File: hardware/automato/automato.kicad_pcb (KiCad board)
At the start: 2 copper layers, 100 x 55.5 mm, 25 parts, among them J2 Motor_L, J3 Motor_3, J5 Servo 1, J6 i2c, U1 ESP32-C6-DEVKITC-1-N8, U2 DRV8411APWPR, U3 AP63357DV-7

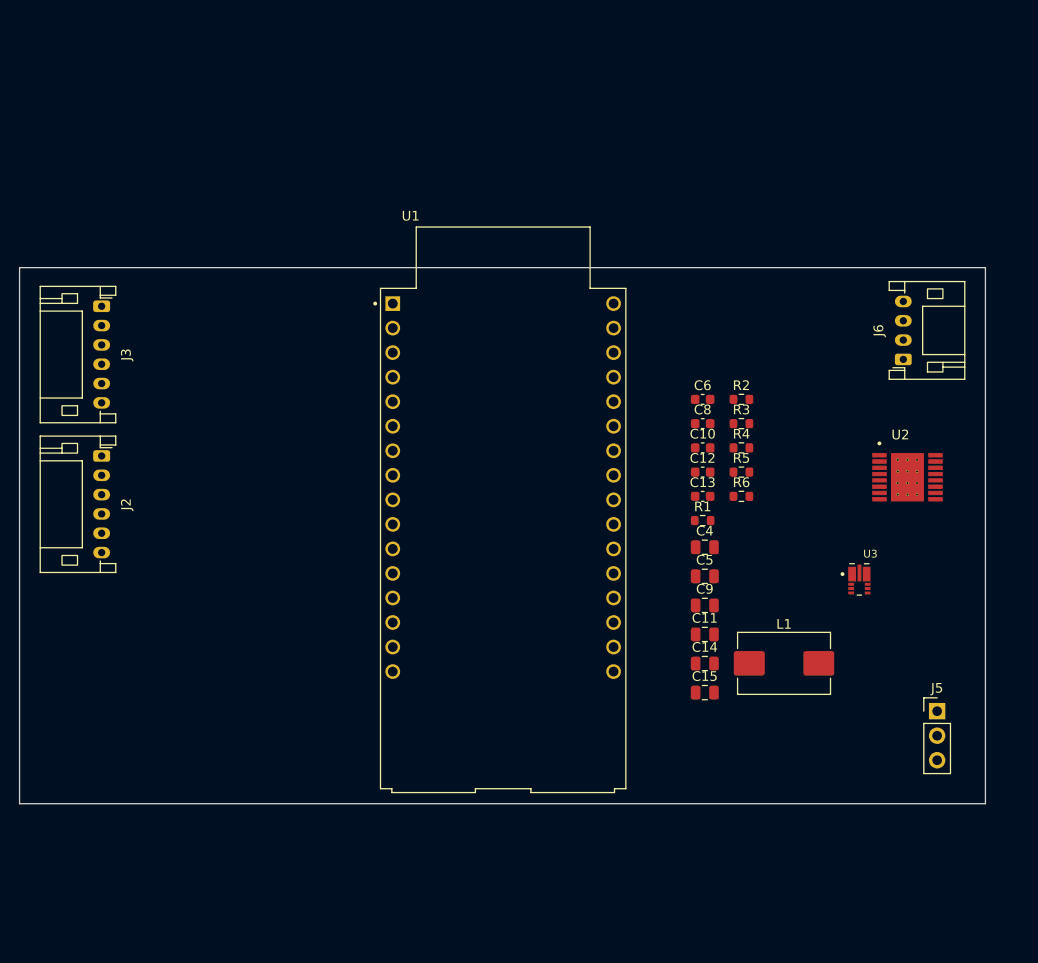
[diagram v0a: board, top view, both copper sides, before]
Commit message: added relays and mosfets
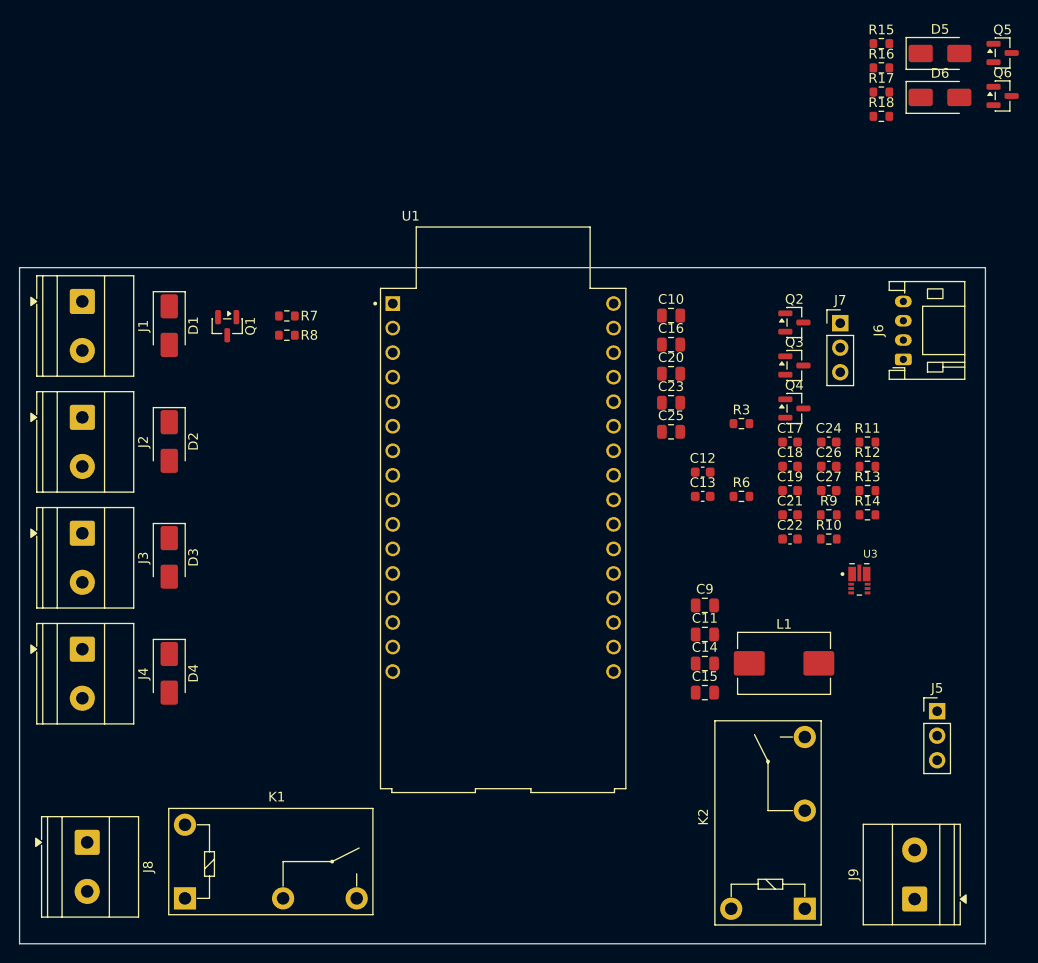
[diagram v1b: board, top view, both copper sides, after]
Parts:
- removed C4, C5: 22uF, Capacitor_SMD:C_0805_2012Metric
- removed C6, C8: 0.1uf, Capacitor_SMD:C_0603_1608Metric
- removed R1, R2: 100k, Resistor_SMD:R_0603_1608Metric
- removed R4, R5: 5.1k, Resistor_SMD:R_0603_1608Metric
- removed U2: DRV8411APWPR, Kjelland:IC_DRV8411APWPR
- added C16: 22uF, Capacitor_SMD:C_0805_2012Metric, F.Cu at (167.9, 102.5)
- added C17: 0.1uF, Capacitor_SMD:C_0603_1608Metric, F.Cu at (180.3, 112.6)
- added C18: 0.1uF, Capacitor_SMD:C_0603_1608Metric, F.Cu at (180.3, 115.1)
- added C19: 0.1uF, Capacitor_SMD:C_0603_1608Metric, F.Cu at (180.3, 117.6)
- added C20: 22uF, Capacitor_SMD:C_0805_2012Metric, F.Cu at (167.9, 105.5)
- added C21: 0.1uF, Capacitor_SMD:C_0603_1608Metric, F.Cu at (180.3, 120.1)
- added C22: 0.1uF, Capacitor_SMD:C_0603_1608Metric, F.Cu at (180.3, 122.6)
- added C23: 22uF, Capacitor_SMD:C_0805_2012Metric, F.Cu at (167.9, 108.5)
- added C24: 0.1uF, Capacitor_SMD:C_0603_1608Metric, F.Cu at (184.3, 112.6)
- added C25: 22uF, Capacitor_SMD:C_0805_2012Metric, F.Cu at (167.9, 111.5)
- added C26: 0.1uF, Capacitor_SMD:C_0603_1608Metric, F.Cu at (184.3, 115.1)
- added C27: 0.1uF, Capacitor_SMD:C_0603_1608Metric, F.Cu at (184.3, 117.6)
- added D1: SS34, Diode_SMD:D_SMA, F.Cu at (116.0, 100.5)
- added D2: SS34, Diode_SMD:D_SMA, F.Cu at (116.0, 112.5)
- added D3: SS34, Diode_SMD:D_SMA, F.Cu at (116.0, 124.5)
- added D4: SS34, Diode_SMD:D_SMA, F.Cu at (116.0, 136.5)
- added D5: SS34, Diode_SMD:D_SMA, F.Cu at (195.8, 72.3)
- added D6: SS34, Diode_SMD:D_SMA, F.Cu at (195.8, 76.9)
- added J1: Motor1, TerminalBlock_Phoenix:TerminalBlock_Phoenix_MKDS-1,5-2-5.08_1x02_P5.08mm_Horizontal, F.Cu at (107.0, 98.0)
- added J4: Motor3, TerminalBlock_Phoenix:TerminalBlock_Phoenix_MKDS-1,5-2-5.08_1x02_P5.08mm_Horizontal, F.Cu at (107.0, 134.0)
- added J7: Servo 2, Connector_PinHeader_2.54mm:PinHeader_1x03_P2.54mm_Vertical, F.Cu at (185.5, 100.2)
- added J8: Relay 1, TerminalBlock_Phoenix:TerminalBlock_Phoenix_MKDS-1,5-2-5.08_1x02_P5.08mm_Horizontal, F.Cu at (107.5, 154.0)
- added J9: Relay 2, TerminalBlock_Phoenix:TerminalBlock_Phoenix_MKDS-1,5-2-5.08_1x02_P5.08mm_Horizontal, F.Cu at (193.2, 159.9)
- added K1: G5Q-1A, Relay_THT:Relay_SPST_Omron-G5Q-1A, F.Cu at (117.6, 159.8)
- added K2: G5Q-1A, Relay_THT:Relay_SPST_Omron-G5Q-1A, F.Cu at (181.8, 160.9)
- added Q1: AO3400A, Package_TO_SOT_SMD:SOT-23, F.Cu at (122.0, 100.6)
- added Q2: AO3400A, Package_TO_SOT_SMD:SOT-23, F.Cu at (180.7, 100.2)
- added Q3: AO3400A, Package_TO_SOT_SMD:SOT-23, F.Cu at (180.7, 104.6)
- added Q4: AO3400A, Package_TO_SOT_SMD:SOT-23, F.Cu at (180.7, 109.1)
- added Q5: AO3400A, Package_TO_SOT_SMD:SOT-23, F.Cu at (202.3, 72.3)
- added Q6: AO3400A, Package_TO_SOT_SMD:SOT-23, F.Cu at (202.3, 76.7)
- added R10: 10k, Resistor_SMD:R_0603_1608Metric, F.Cu at (184.3, 122.6)
- added R11: 120R, Resistor_SMD:R_0603_1608Metric, F.Cu at (188.3, 112.6)
- added R12: 10k, Resistor_SMD:R_0603_1608Metric, F.Cu at (188.3, 115.1)
- added R13: 120R, Resistor_SMD:R_0603_1608Metric, F.Cu at (188.3, 117.6)
- added R14: 10k, Resistor_SMD:R_0603_1608Metric, F.Cu at (188.3, 120.1)
- added R15: 120R, Resistor_SMD:R_0603_1608Metric, F.Cu at (189.7, 71.3)
- added R16: 10k, Resistor_SMD:R_0603_1608Metric, F.Cu at (189.7, 73.8)
- added R17: 120R, Resistor_SMD:R_0603_1608Metric, F.Cu at (189.7, 76.3)
- added R18: 10k, Resistor_SMD:R_0603_1608Metric, F.Cu at (189.7, 78.8)
- added R7: 120R, Resistor_SMD:R_0603_1608Metric, F.Cu at (128.2, 99.5)
- added R8: 10k, Resistor_SMD:R_0603_1608Metric, F.Cu at (128.2, 101.5)
- added R9: 120R, Resistor_SMD:R_0603_1608Metric, F.Cu at (184.3, 120.1)
- C10: value 0.1uf -> 22uF; footprint Capacitor_SMD:C_0603_1608Metric -> Capacitor_SMD:C_0805_2012Metric
- J2: value Motor_L -> Motor2; footprint Connector_JST:JST_PH_S6B-PH-K_1x06_P2.00mm_Horizontal -> TerminalBlock_Phoenix:TerminalBlock_Phoenix_MKDS-1,5-2-5.08_1x02_P5.08mm_Horizontal
- J3: value Motor_3 -> Motor4; footprint Connector_JST:JST_PH_S6B-PH-K_1x06_P2.00mm_Horizontal -> TerminalBlock_Phoenix:TerminalBlock_Phoenix_MKDS-1,5-2-5.08_1x02_P5.08mm_Horizontal
- moved J3 23.6 mm to (107.0, 122.0)
- moved C10 14.1 mm to (167.9, 99.5)
- moved J2 4.47 mm to (107.0, 110.0)
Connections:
- C10 pad 1: /MOTOR_L_A -> +5V
- C11 pad 1: +9V -> +12V
- J2 pad 1: /MOTOR_L_OUT+ -> +12V
- J2 pad 2: /MOTOR_L_OUT- -> Net-(D2-A)
- J3 pad 1: /MOTOR_3_OUT+ -> +12V
- J3 pad 2: /MOTOR_3_OUT- -> Net-(D3-A)
- J5 pad 1: /SERVO_1 -> SERVO_1
- U1 pad J1_12: /ENC_LB -> unconnected-(U1-GPIO14-PadJ1_12)
- U1 pad J1_3: /SERVO_1 -> SERVO_2
- U1 pad J1_4: unconnected-(U1-GPIO3-PadJ1_4) -> MOTOR_1
- U1 pad J1_5: unconnected-(U1-GPIO4-PadJ1_5) -> MOTOR_2
- U1 pad J1_6: unconnected-(U1-GPIO5-PadJ1_6) -> MOTOR_3
- U1 pad J1_7: /MOTOR_L_A -> MOTOR_4
- U1 pad J1_8: /MOTOR_3_A -> SERVO_1
- U1 pad J1_9: /ENC_LA -> unconnected-(U1-GPIO8-PadJ1_9)
- U1 pad J3_4: /ENC_3A -> unconnected-(U1-GPIO23-PadJ3_4)
- U1 pad J3_5: /ENC_3B -> unconnected-(U1-GPIO22-PadJ3_5)
- U1 pad J3_6: /MOTOR_3_IN2 -> unconnected-(U1-GPIO21-PadJ3_6)
- U1 pad J3_7: /MOTOR_3_IN1 -> unconnected-(U1-GPIO20-PadJ3_7)
- U1 pad J3_8: /MOTOR_L_IN2 -> unconnected-(U1-GPIO19-PadJ3_8)
- U1 pad J3_9: /MOTOR_L_IN1 -> unconnected-(U1-GPIO18-PadJ3_9)
- U3 pad 1: +9V -> +12V
- U3 pad 2: +9V -> +12V
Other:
- board size 100 x 55.5 mm -> 100 x 70 mm

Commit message: started layout
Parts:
- added C28: 22uF, Capacitor_SMD:C_0805_2012Metric, F.Cu at (236.5, 66.0)
- added C29: 22uF, Capacitor_SMD:C_0805_2012Metric, F.Cu at (236.5, 71.0)
- added FID1: Fiducial, Fiducial:Fiducial_1.5mm_Mask3mm, F.Cu at (233.5, 47.0)
- added FID2: Fiducial, Fiducial:Fiducial_1.5mm_Mask3mm, F.Cu at (161.0, 45.5)
- added FID3: Fiducial, Fiducial:Fiducial_1.5mm_Mask3mm, F.Cu at (242.5, 119.5)
- added FID4: Fiducial, Fiducial:Fiducial_1.5mm_Mask3mm, F.Cu at (182.0, 128.0)
- added H1: MountingHole, MountingHole:MountingHole_3.2mm_M3, F.Cu at (152.0, 129.0)
- added H2: MountingHole, MountingHole:MountingHole_3.2mm_M3, F.Cu at (152.0, 45.0)
- added H3: MountingHole, MountingHole:MountingHole_3.2mm_M3, F.Cu at (246.0, 45.0)
- added H4: MountingHole, MountingHole:MountingHole_3.2mm_M3, F.Cu at (246.0, 129.0)
- added J10: Servo 3, Connector_PinHeader_2.54mm:PinHeader_1x03_P2.54mm_Vertical, F.Cu at (241.9, 66.0)
- added J11: Servo 4, Connector_PinHeader_2.54mm:PinHeader_1x03_P2.54mm_Vertical, F.Cu at (241.9, 71.0)
- added J12: Barrel_Jack, Connector_BarrelJack:BarrelJack_Horizontal, F.Cu at (163.0, 120.3)
- added R19: 4.7k, Resistor_SMD:R_0603_1608Metric, F.Cu at (163.5, 108.0)
- added R20: 4.7k, Resistor_SMD:R_0603_1608Metric, F.Cu at (163.5, 105.0)
- moved J8 114.1 mm to (217.0, 122.0), turned to 0 degrees
- moved C17 109.2 mm to (97.3, 41.6)
- moved C19 109.2 mm to (97.3, 46.6)
- moved C22 109.2 mm to (97.3, 51.6)
- moved C16 109.2 mm to (85.0, 31.5)
- moved C20 109.2 mm to (85.0, 34.5)
- moved C23 109.2 mm to (85.0, 37.5)
- moved C24 109.2 mm to (101.3, 41.6)
- moved C25 109.2 mm to (85.0, 40.5)
- moved C9 98.2 mm to (236.5, 56.0), turned to -90 degrees
- moved J5 96.3 mm to (241.9, 56.0), turned to 90 degrees
- moved K1 96.3 mm to (201.8, 113.0)
- moved C10 78.6 mm to (236.5, 61.0), turned to -90 degrees
- moved D4 74.4 mm to (165.0, 80.5)
- moved J4 74.4 mm to (156.0, 78.0)
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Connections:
- net /SCL renamed SCL
- net /SDA renamed SDA
- U1 pad J1_12: unconnected-(U1-GPIO14-PadJ1_12) -> RELAY_1
- U1 pad J1_13: unconnected-(U1-GND-PadJ1_13) -> GND
- U1 pad J1_15: unconnected-(U1-GND_J1_15-PadJ1_15) -> GND
- U1 pad J1_3: SERVO_2 -> SERVO_3
- U1 pad J1_4: MOTOR_1 -> SERVO_4
- U1 pad J1_5: MOTOR_2 -> unconnected-(U1-GPIO4-PadJ1_5)
- U1 pad J1_6: MOTOR_3 -> unconnected-(U1-GPIO5-PadJ1_6)
- U1 pad J1_7: MOTOR_4 -> RELAY_1
- U1 pad J1_8: SERVO_1 -> RELAY_2
- U1 pad J3_1: unconnected-(U1-GND_J3_1-PadJ3_1) -> GND
- U1 pad J3_12: unconnected-(U1-GND_J3_12-PadJ3_12) -> GND
- U1 pad J3_15: unconnected-(U1-GND_J3_15-PadJ3_15) -> GND
- U1 pad J3_4: unconnected-(U1-GPIO23-PadJ3_4) -> SERVO_1
- U1 pad J3_5: unconnected-(U1-GPIO22-PadJ3_5) -> SERVO_2
- U1 pad J3_6: unconnected-(U1-GPIO21-PadJ3_6) -> MOTOR_1
- U1 pad J3_7: unconnected-(U1-GPIO20-PadJ3_7) -> MOTOR_2
- U1 pad J3_8: unconnected-(U1-GPIO19-PadJ3_8) -> MOTOR_3
- U1 pad J3_9: unconnected-(U1-GPIO18-PadJ3_9) -> MOTOR_4
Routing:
- net GND: track 0.00 -> 8.71 mm, vias 0 -> 2
- net Net-(U3-SW): track 0.00 -> 6.16 mm, vias 0 -> 2
- net +12V: track 0.00 -> 4.26 mm
- net Net-(U3-FB): track 0.00 -> 3.11 mm
- net Net-(U3-BST): track 0.00 -> 2.78 mm
- added copper zone on F.Cu, net +12V
- added copper zone on B.Cu, net GND
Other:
- board size 100 x 70 mm -> 100 x 90 mm

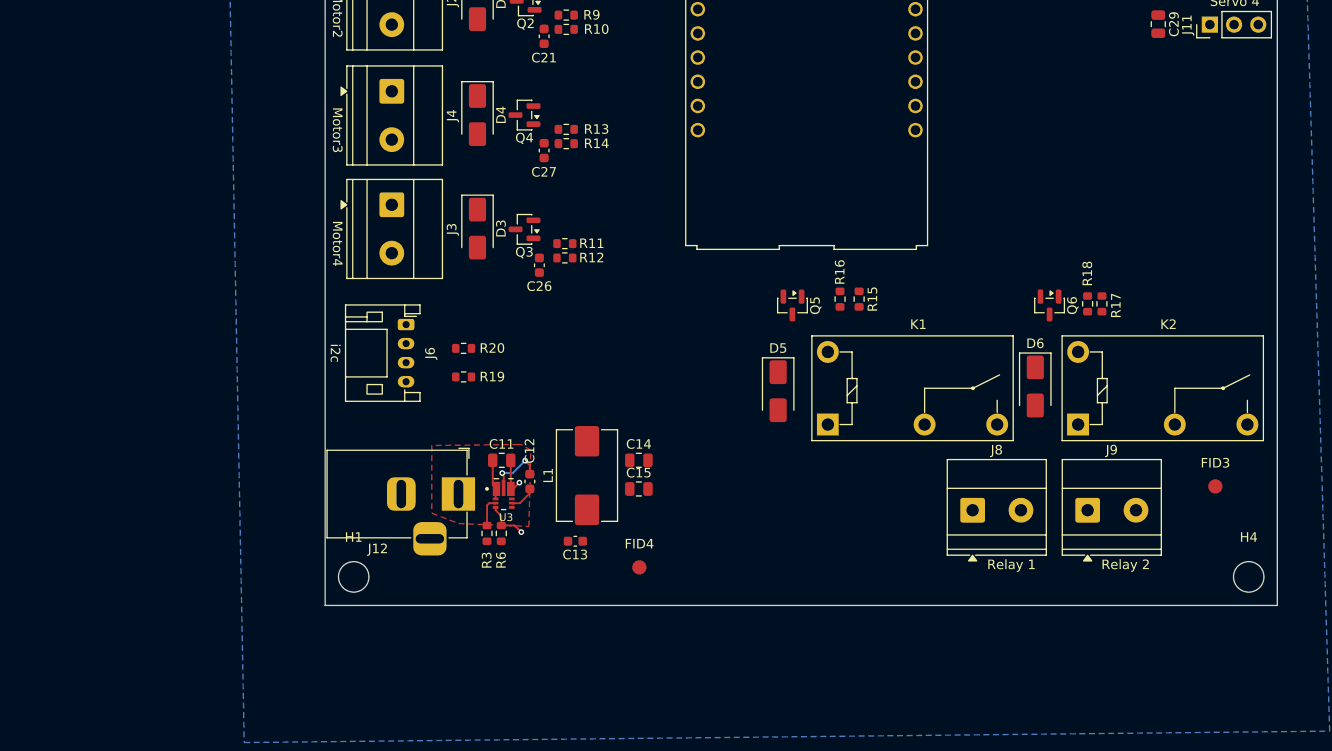
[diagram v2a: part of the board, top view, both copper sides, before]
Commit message: changed 5v power supply
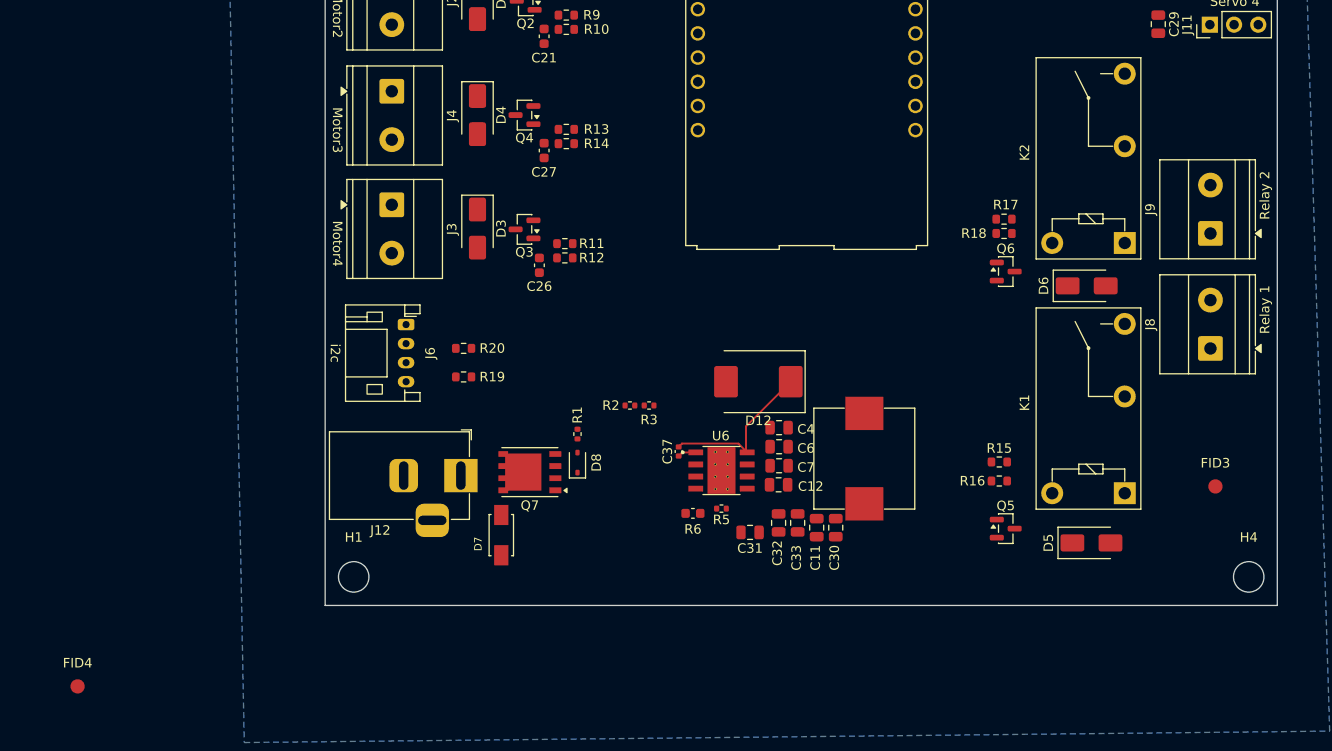
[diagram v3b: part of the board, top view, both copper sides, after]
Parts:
- removed C13: 47pF, Capacitor_SMD:C_0603_1608Metric
- removed C14, C15: 22uF, Capacitor_SMD:C_0805_2012Metric
- removed L1: 6.8uH, Inductor_SMD:L_Wuerth_HCM-1078
- removed U3: AP63357DV-7, Kjelland:CONV_AP63357DV-7
- added C30: 47uF, Capacitor_SMD:C_0805_2012Metric, F.Cu at (202.6, 123.8)
- added C31: 47uF, Capacitor_SMD:C_0805_2012Metric, F.Cu at (193.6, 124.3)
- added C32: 47uF, Capacitor_SMD:C_0805_2012Metric, F.Cu at (196.6, 123.3)
- added C33: 47uF, Capacitor_SMD:C_0805_2012Metric, F.Cu at (198.6, 123.3)
- added C37: 10nF (LOW ESR), Capacitor_SMD:C_0402_1005Metric, F.Cu at (186.1, 115.8)
- added C4: 2.2uF, Capacitor_SMD:C_0805_2012Metric, F.Cu at (196.7, 113.3)
- added C6: 2.2uF, Capacitor_SMD:C_0805_2012Metric, F.Cu at (196.7, 115.3)
- added C7: 2.2uF, Capacitor_SMD:C_0805_2012Metric, F.Cu at (196.7, 117.3)
- added D12: SM540C, Diode_SMD:D_SMC, F.Cu at (194.5, 108.5)
- added D7: SMAJ16CA-13-F, BlackPanda:DIOM4325X250N, F.Cu at (167.5, 124.6)
- added D8: BAS40WS 43, Diode_SMD:D_SOD-323, F.Cu at (175.5, 117.0)
- added L4: 15uH, BlackPanda:L_10.5x11.5_H4.0, F.Cu at (205.6, 116.6)
- added Q7: HY12P03C2, Package_SO:PowerPAK_SO-8_Single, F.Cu at (170.5, 118.0)
- added R1: 1K, Resistor_SMD:R_0402_1005Metric, F.Cu at (175.5, 114.0)
- added R2: 1K, Resistor_SMD:R_0402_1005Metric, F.Cu at (181.0, 111.0)
- added R5: 10K (1%), Resistor_SMD:R_0402_1005Metric, F.Cu at (190.6, 121.8)
- added U6: TPS5450DDAR, BlackPanda:CONV_TPS5450DDAR, F.Cu at (190.6, 117.8)
- C11: value 22uF -> 47uF
- C12: value 0.1uF -> 2.2uF; footprint Capacitor_SMD:C_0603_1608Metric -> Capacitor_SMD:C_0805_2012Metric
- R3: value 180k -> 10K; footprint Resistor_SMD:R_0603_1608Metric -> Resistor_SMD:R_0402_1005Metric
- R6: value 33k -> 3.16K (1%); footprint Resistor_SMD:R_0603_1608Metric -> Capacitor_SMD:C_0603_1608Metric
- moved FID4 60.3 mm to (123.0, 140.5)
- moved D5 36.6 mm to (229.5, 125.4), turned to 0 degrees
- moved C11 33.8 mm to (200.6, 123.8), turned to 90 degrees
- moved Q5 32.4 mm to (220.5, 123.9), turned to 0 degrees
- moved K1 32.0 mm to (233.0, 120.2), turned to 90 degrees
- moved J9 31.8 mm to (242.0, 92.9), turned to 90 degrees
- moved J8 30.2 mm to (242.0, 105.0), turned to 90 degrees
- moved C12 26.1 mm to (196.6, 119.3), turned to 0 degrees
- moved R16 25.4 mm to (219.8, 118.9), turned to 0 degrees
- moved R15 22.6 mm to (219.8, 116.9), turned to 0 degrees
- moved R3 21.7 mm to (183.0, 111.0), turned to 0 degrees
- moved R6 20.2 mm to (187.6, 122.3), turned to 0 degrees
- moved K2 19.7 mm to (233.0, 93.9), turned to 90 degrees
- moved R17 13.6 mm to (220.3, 91.4), turned to 0 degrees
- moved D6 11.9 mm to (229.0, 98.4), turned to 0 degrees
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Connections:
- C11 pad 1: +12V -> GND
- C11 pad 2: GND -> +5V
- C12 pad 1: Net-(U3-BST) -> +12V
- C12 pad 2: Net-(U3-SW) -> GND
- J12 pad 1: +12V -> Net-(Q7-D)
- R3 pad 1: +5V -> VoltageSens
- R3 pad 2: Net-(U3-FB) -> +12V
- R6 pad 1: Net-(U3-FB) -> GND
- R6 pad 2: GND -> VSENSE
- U1 pad J1_5: unconnected-(U1-GPIO4-PadJ1_5) -> VoltageSens
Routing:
- net /L4: track 0.00 -> 17.2 mm
- net GND: track 8.71 -> 0.00 mm, vias 2 -> 0
- net Net-(U3-SW): track 6.16 -> 0.00 mm, vias 2 -> 0
- net +12V: track 4.26 -> 0.00 mm
- net Net-(U3-FB): track 3.11 -> 0.00 mm
- net Net-(U3-BST): track 2.78 -> 0.00 mm
- net Net-(U6-BOOT): track 0.00 -> 1.96 mm
- removed copper zone on F.Cu, net +12V
